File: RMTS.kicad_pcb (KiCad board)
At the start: 2 copper layers, 45 parts, among them J1 USB_B_Mini, J2 Programmer, J3 Screw_Terminal_01x03, J4 Screw_Terminal_01x04, J5 Screw_Terminal_01x02, J6 Screw_Terminal_01x02, J7 MICRO-SD_CARD_SOCKET, J8 CONN_03, Q1 PMV20ENR, U1 ADP2108AUJ-3.3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

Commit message: Finished layout
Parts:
- added C14: 12pF, Capacitor_SMD:C_0805_2012Metric_Pad1.15x1.40mm_HandSolder, F.Cu at (182.9, 102.9)
- added C15: 12pF, Capacitor_SMD:C_0805_2012Metric_Pad1.15x1.40mm_HandSolder, F.Cu at (182.6, 95.2)
- added C16: 0.1uF, Capacitor_SMD:C_0805_2012Metric_Pad1.15x1.40mm_HandSolder, F.Cu at (163.4, 81.9)
- added J10: CONN_02, Connectors:1X02, F.Cu at (141.6, 99.7)
- added J9: CONN_02, Connectors:1X02, F.Cu at (147.3, 99.7)
- added Y2: Crystal_GND24_Small, Crystal:Crystal_SMD_3225-4Pin_3.2x2.5mm, F.Cu at (183.1, 99.1)
- J7: value MICRO-SD_CARD_SOCKET -> Micro_SD_Card_Det_Hirose_DM3AT; footprint Connectors:MICRO-SD-SOCKET -> Connector_Card:microSD_HC_Hirose_DM3AT-SF-PEJM5
- moved C12 14.6 mm to (197.9, 89.5), turned to 180 degrees
- moved C1 11.4 mm to (142.2, 72.0), turned to 90 degrees
- moved R5 10.8 mm to (205.5, 92.1)
- moved TP2 10.0 mm to (151.8, 78.1)
- moved C13 9.17 mm to (201.5, 68.6), turned to 180 degrees
- moved J7 8.60 mm to (167.2, 71.7), turned to 180 degrees
- moved C2 8.26 mm to (153.3, 73.0)
- moved R2 7.92 mm to (146.3, 80.0), turned to 180 degrees
- moved U1 7.15 mm to (146.1, 72.1)
- moved L1 6.96 mm to (146.6, 76.2)
- moved C11 6.47 mm to (202.2, 89.5)
- moved U3 6.37 mm to (199.4, 97.8)
- moved Q1 5.65 mm to (146.4, 95.6)
- moved J1 5.31 mm to (134.6, 73.3)
- moved R8 5.28 mm to (193.7, 97.5)
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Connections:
- net Net-(U2-Pad32) renamed /XTAL1
- net Net-(U2-Pad33) renamed /XTAL2
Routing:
- net +3V3: track 9.50 -> 186.6 mm, vias 0 -> 4
- net GND: track 0.00 -> 124.1 mm, vias 0 -> 17
- net /VBUS: track 0.00 -> 118.0 mm, vias 0 -> 2
- net /DIN: track 0.00 -> 40.0 mm
- net /DOUT: track 0.00 -> 37.9 mm
- net Net-(D2-Pad2): track 0.00 -> 28.3 mm, vias 0 -> 2
- net /USBM: track 0.00 -> 21.7 mm
- net /Fire: track 0.00 -> 20.6 mm, vias 0 -> 2
- net Net-(D1-Pad2): track 0.00 -> 20.0 mm
- net /USBP: track 0.00 -> 16.9 mm
- net Net-(J1-Pad3): track 0.00 -> 15.0 mm
- net Net-(J4-Pad4): track 0.00 -> 14.2 mm
- net Net-(J3-Pad3): track 0.00 -> 14.1 mm
- net Net-(J1-Pad2): track 0.00 -> 12.5 mm
- net /LC0: track 0.00 -> 11.9 mm
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- added copper zone on B.Cu, net GND
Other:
- board outline added: 79.4 x 50.2 mm

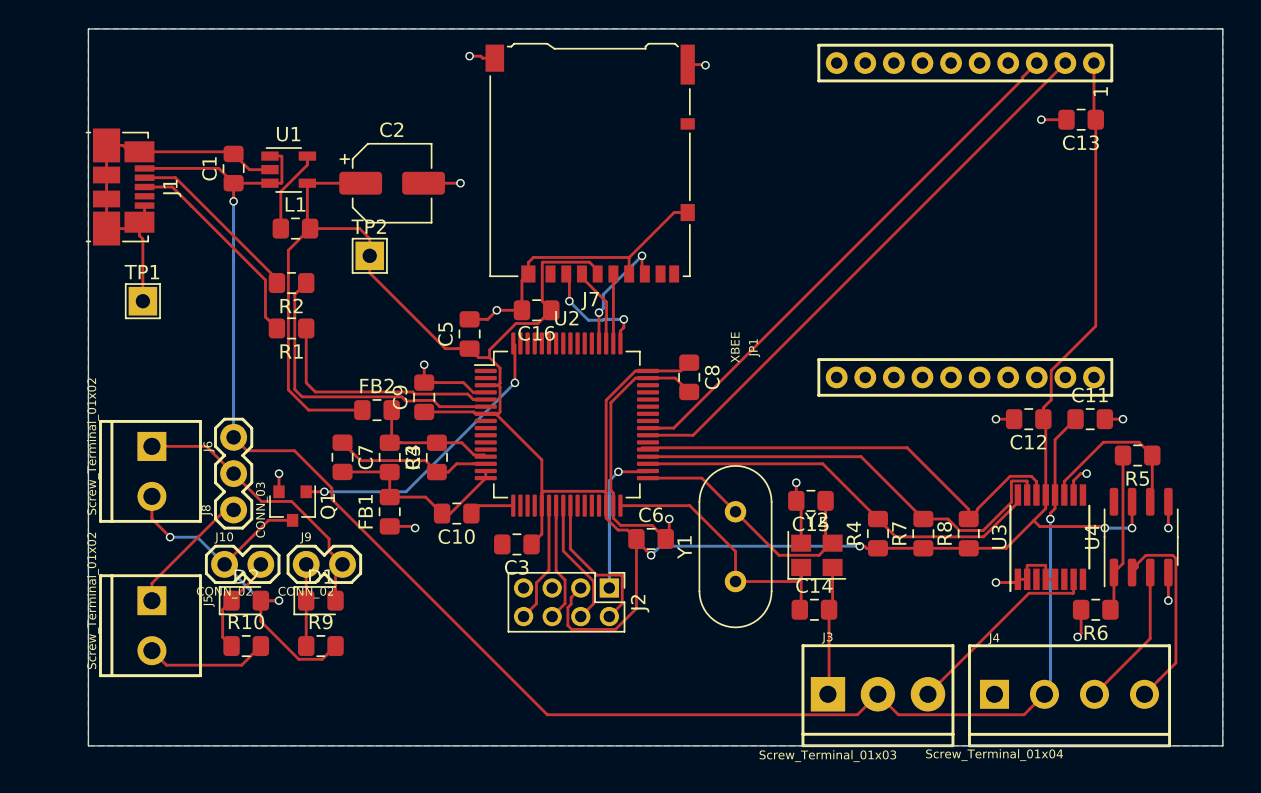
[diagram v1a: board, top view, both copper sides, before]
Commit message: Cleaned up silkscreen
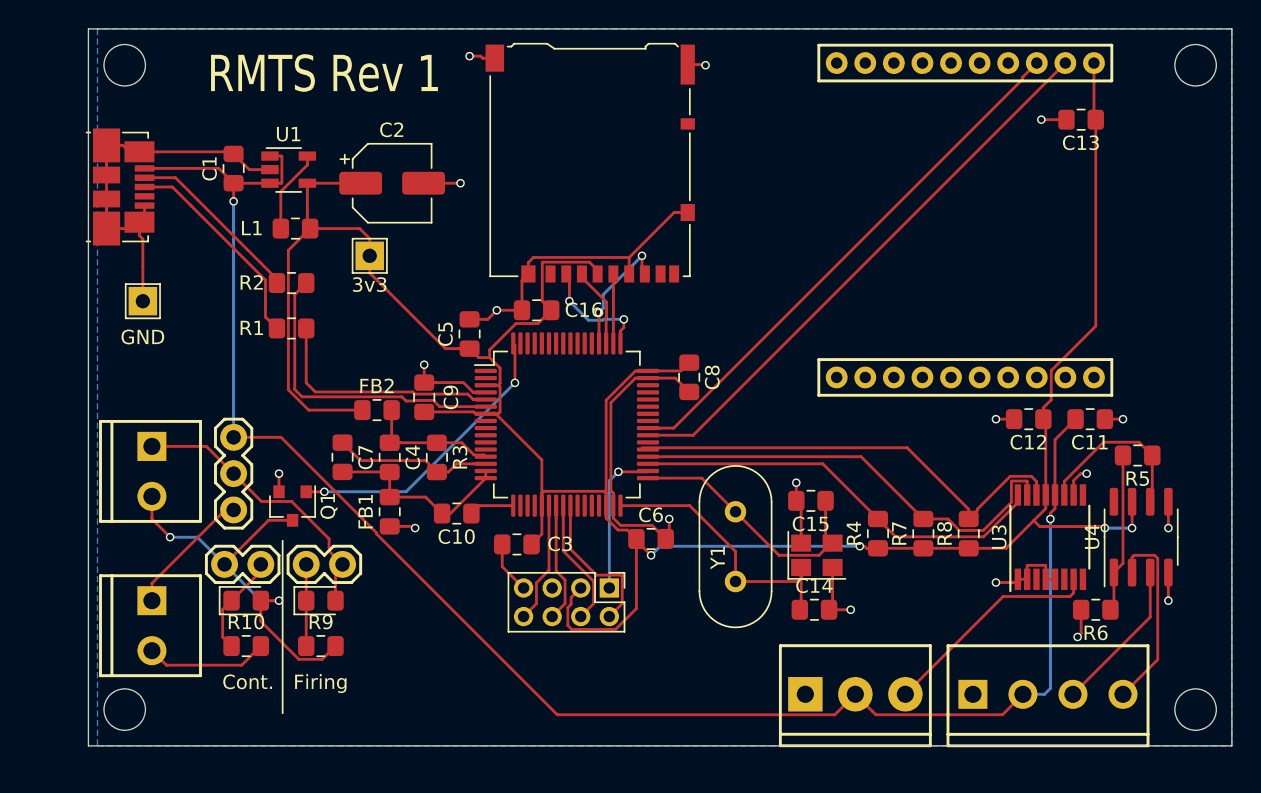
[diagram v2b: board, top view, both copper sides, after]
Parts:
- TP1: value TestPoint -> GND
- TP2: value TestPoint -> 3v3
- moved J3 1.58 mm to (182.2, 108.8)
- moved J4 1.51 mm to (194.0, 108.8)
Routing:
- net Net-(J3-Pad3): track 14.1 -> 15.7 mm
- net GND: track 124.1 -> 123.3 mm, vias 17 -> 18
- net Net-(J4-Pad4): track 14.2 -> 13.5 mm
- net Net-(J4-Pad3): track 10.1 -> 10.8 mm
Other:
- board size 79.4 x 50.2 mm -> 80 x 50.2 mm
- board text added: "Cont."
- board text added: "Firing"
- board text added: "RMTS Rev 1"

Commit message: Added label to screw terminals
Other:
- board text added: "+"
- board text added: "-"
- board text added: "Igniter"
- board text added: "SIG"
- board text added: "SIG+"
- board text added: "SIG-"
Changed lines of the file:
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@@
   (general
     (thickness 1.6)
-    (drawings 12)
+    (drawings 22)
     (tracks 462)
     (zones 0)
@@
     (solder_mask_min_width 0.25)
     (aux_axis_origin 0 0)
-    (visible_elements 7FFFFFFF)
+    (visible_elements 7FFDFFFF)
     (pcbplotparams
       (layerselection 0x010fc_ffffffff)
@@
       (net 10 "Net-(D2-Pad2)") (solder_mask_margin 0.1016))
   )
+  (gr_text Igniter (at 133.858 93.218 -90) (layer B.SilkS)
+    (effects (font (size 1 1) (thickness 0.15)) (justify mirror))
+  )
+  (gr_text + (at 133.985 102.235 90) (layer B.SilkS)
+    (effects (font (size 1 1) (thickness 0.15)) (justify mirror))
+  )
+  (gr_text - (at 133.858 105.791 90) (layer B.SilkS)
+    (effects (font (size 1 1) (thickness 0.15)) (justify mirror))
+  )
+  (gr_text SIG- (at 204.216 110.998) (layer B.SilkS)
+    (effects (font (size 1 1) (thickness 0.15)) (justify mirror))
+  )
+  (gr_text SIG+ (at 200.406 110.998) (layer B.SilkS)
+    (effects (font (size 1 1) (thickness 0.15)) (justify mirror))
+  )
+  (gr_text + (at 197.485 110.998) (layer B.SilkS)
+    (effects (font (size 1 1) (thickness 0.15)) (justify mirror))
+  )
+  (gr_text - (at 193.929 110.998) (layer B.SilkS)
+    (effects (font (size 1 1) (thickness 0.15)) (justify mirror))
+  )
+  (gr_text SIG (at 189.23 111.125) (layer B.SilkS)
+    (effects (font (size 1 1) (thickness 0.15)) (justify mirror))
+  )
+  (gr_text + (at 185.801 111.125) (layer B.SilkS)
+    (effects (font (size 1 1) (thickness 0.15)) (justify mirror))
+  )
+  (gr_text - (at 182.245 111.125) (layer B.SilkS)
+    (effects (font (size 1 1) (thickness 0.15)) (justify mirror))
+  )
   (gr_line (start 145.669 98.044) (end 145.669 110.109) (layer F.SilkS) (width 0.12))

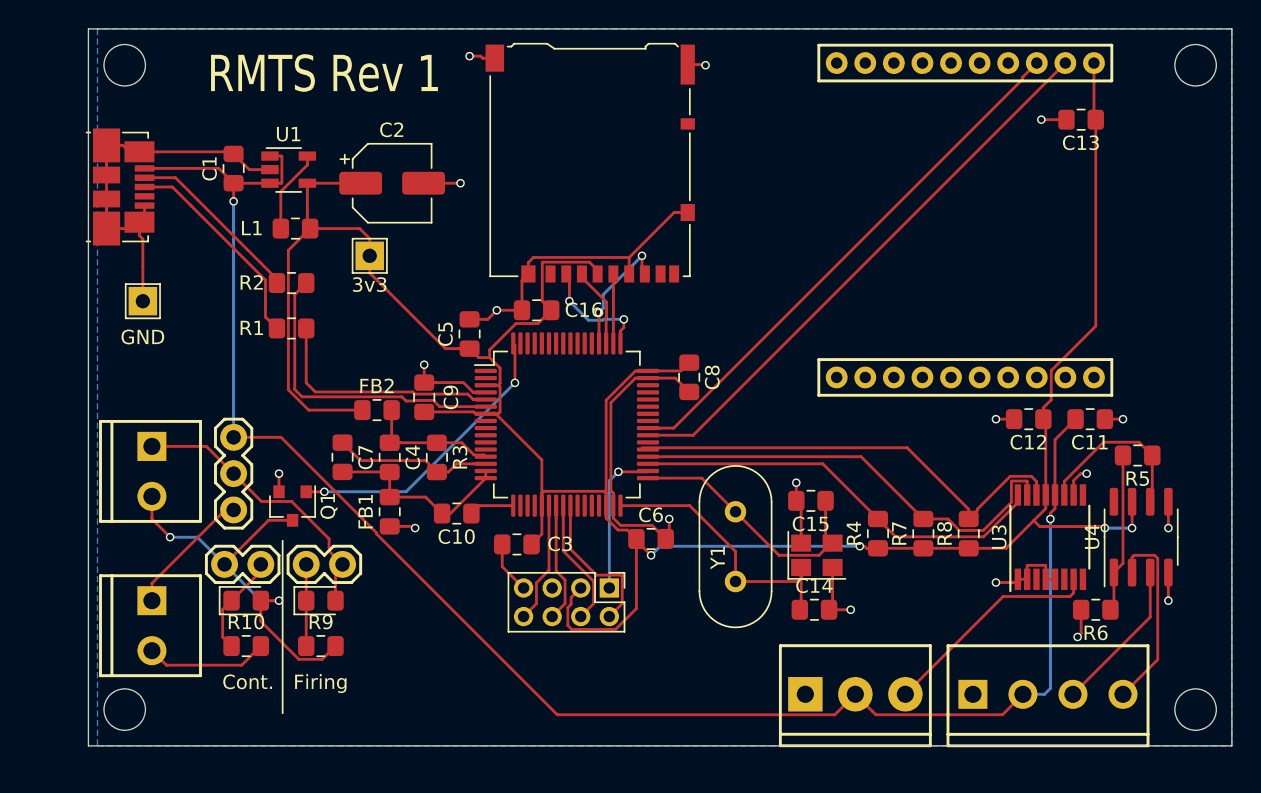
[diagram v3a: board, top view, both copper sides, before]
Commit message: Added 3v3 top plane
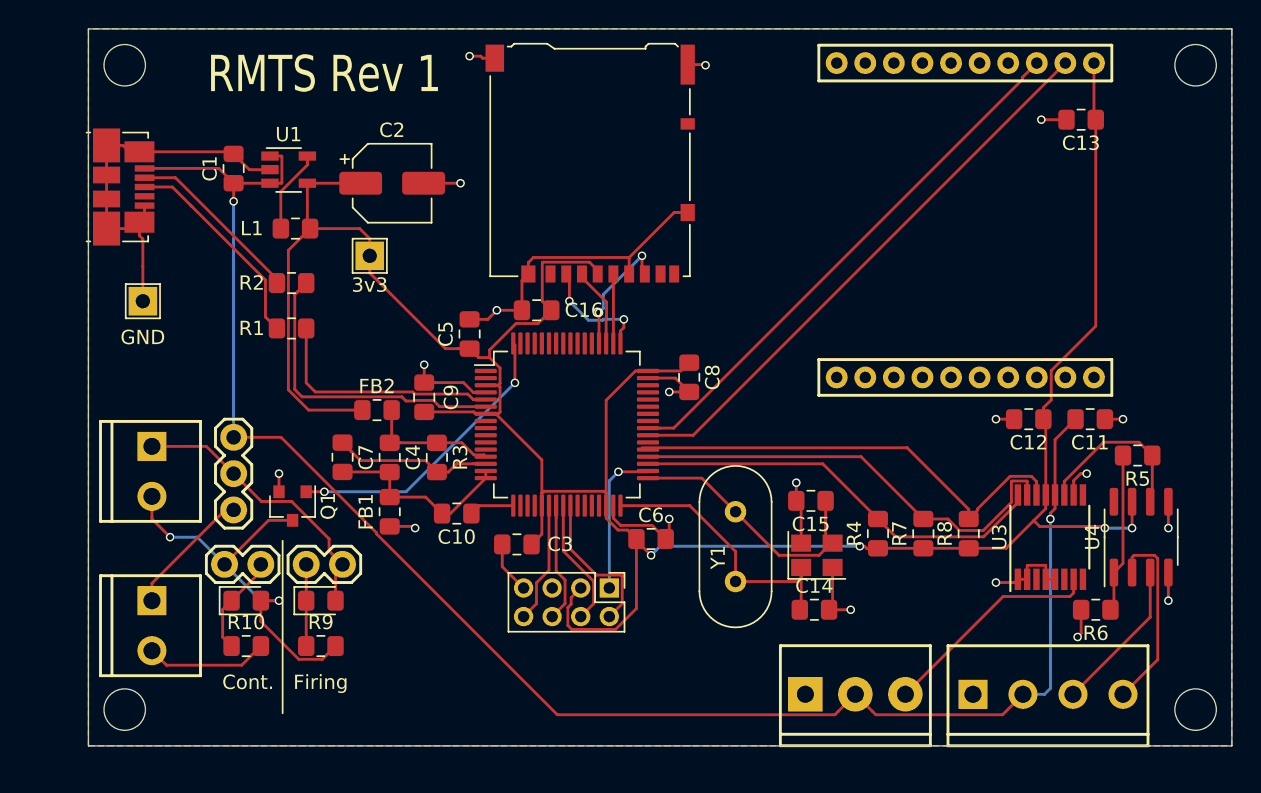
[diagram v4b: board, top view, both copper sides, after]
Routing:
- net GND: track 123.3 -> 114.1 mm, vias 18 -> 19
- added copper zone on F.Cu, net +3V3
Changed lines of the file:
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@@
     (thickness 1.6)
     (drawings 22)
-    (tracks 462)
+    (tracks 459)
     (zones 0)
     (modules 51)
@@
   (segment (start 181.95 95.59) (end 181.61 95.25) (width 0.2) (layer F.Cu) (net 1))
   (segment (start 181.95 98.21) (end 181.95 95.59) (width 0.2) (layer F.Cu) (net 1))
-  (segment (start 170.357001 86.660001) (end 171.232001 86.660001) (width 0.2) (layer F.Cu) (net 1))
-  (segment (start 168.636999 88.380003) (end 170.357001 86.660001) (width 0.2) (layer F.Cu) (net 1))
-  (segment (start 168.636999 94.539999) (end 168.636999 88.380003) (width 0.2) (layer F.Cu) (net 1))
-  (segment (start 168.807001 94.710001) (end 168.636999 94.539999) (width 0.2) (layer F.Cu) (net 1))
-  (segment (start 168.807001 95.585001) (end 168.807001 94.710001) (width 0.2) (layer F.Cu) (net 1))
   (segment (start 173.31348 75.075) (end 174.01348 75.075) (width 0.2) (layer F.Cu) (net 1))
   (segment (start 173.065038 75.075) (end 173.31348 75.075) (width 0.2) (layer F.Cu) (net 1))
@@
   (via (at 185.42 102.87) (size 0.6) (drill 0.4) (layers F.Cu B.Cu) (net 1))
   (segment (start 183.905 102.87) (end 185.42 102.87) (width 0.2) (layer F.Cu) (net 1))
+  (via (at 172.72 87.63) (size 0.6) (drill 0.4) (layers F.Cu B.Cu) (net 1))
+  (segment (start 172.72 87.63) (end 174.117 87.63) (width 0.2) (layer F.Cu) (net 1))
   (segment (start 199.715 90.97) (end 201.15 89.535) (width 0.2) (layer F.Cu) (net 2))
   (segment (start 199.715 94.84) (end 199.715 90.97) (width 0.2) (layer F.Cu) (net 2))
@@
     (polygon
       (pts
-        (xy 132.715 62.23) (xy 132.715 112.395) (xy 212.09 112.395) (xy 212.09 62.23)
+        (xy 132.08 62.23) (xy 132.08 112.395) (xy 212.09 112.395) (xy 212.09 62.23)
       )
     )
+  )
+  (zone (net 3) (net_name +3V3) (layer F.Cu) (hatch edge 0.508)
+    (connect_pads (clearance 0.508))
+    (min_thickness 0.254)
+    (fill yes (arc_segments 32) (thermal_gap 0.508) (thermal_bridge_width 0.508))
+    (polygon
+      (pts
+        (xy 132.08 62.23) (xy 132.08 112.395) (xy 212.09 112.395) (xy 212.09 62.23)
+      )
+    )

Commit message: Changed USB to full size, connected amp enable, cleaned up routing
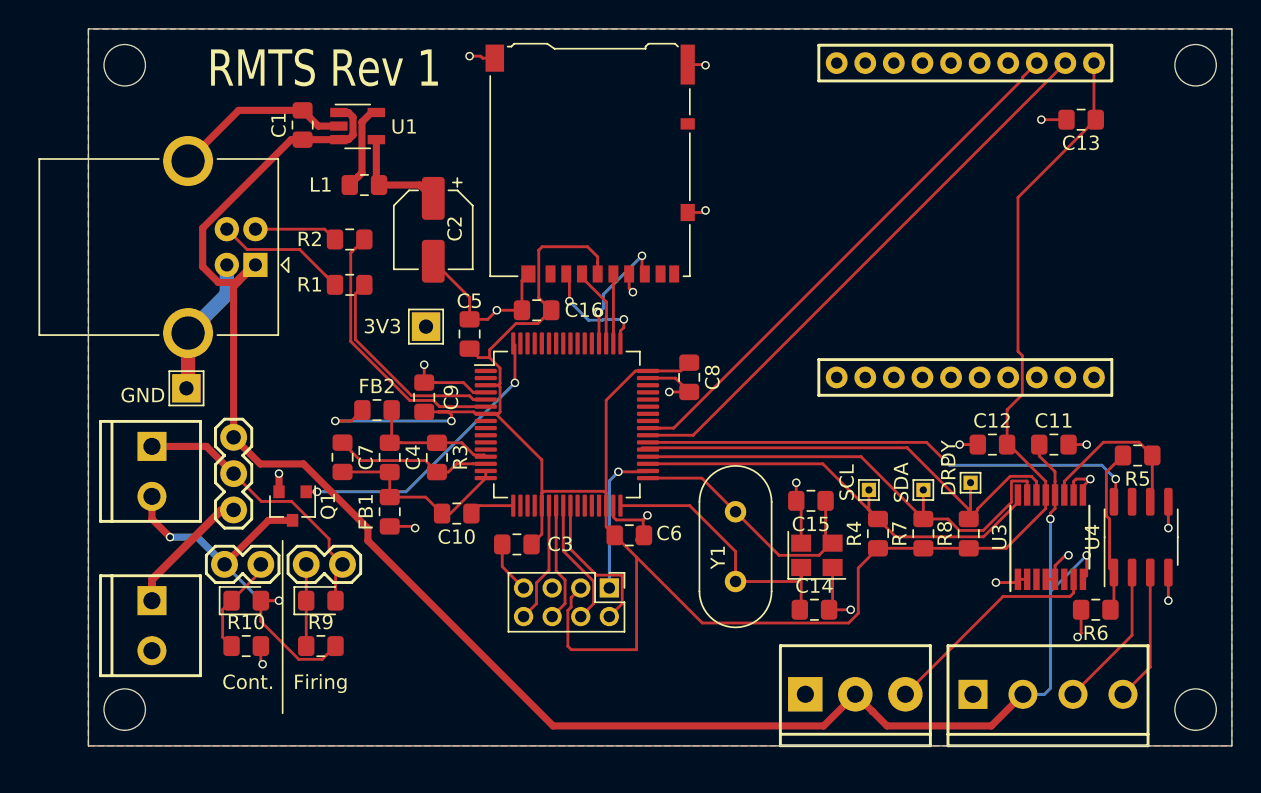
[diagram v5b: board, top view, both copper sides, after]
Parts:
- added DRDY: TestPoint, TestPoint:TestPoint_THTPad_1.0x1.0mm_Drill0.5mm, F.Cu at (193.8, 94.0)
- added SCL: TestPoint, TestPoint:TestPoint_THTPad_1.0x1.0mm_Drill0.5mm, F.Cu at (186.7, 94.5)
- added SDA: TestPoint, TestPoint:TestPoint_THTPad_1.0x1.0mm_Drill0.5mm, F.Cu at (190.5, 94.5)
- J1: value USB_B_Mini -> USB_B; footprint Connector_USB:USB_Micro-B_Molex_47346-0001 -> Connector_USB:USB_B_OST_USB-B1HSxx_Horizontal
- TP2: value 3v3 -> 3V3
- moved J1 10.7 mm to (143.8, 78.7), turned to 180 degrees
- moved TP1 6.82 mm to (138.9, 87.4)
- moved TP2 6.33 mm to (155.7, 83.1)
- moved C1 5.71 mm to (147.1, 69.0)
- moved L1 5.71 mm to (151.4, 73.2)
- moved U1 5.71 mm to (150.9, 69.0)
- moved R1 5.08 mm to (150.4, 80.1)
- moved R2 5.08 mm to (150.4, 77.0)
- moved C2 4.35 mm to (156.2, 76.3), turned to 270 degrees
- moved C11 3.10 mm to (199.6, 91.3)
- moved C12 3.10 mm to (195.3, 91.3)
- moved C6 1.55 mm to (169.9, 97.7)
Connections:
- J1 pad 4: Net-(J1-Pad4) -> GND
- U2 pad 38: Net-(U2-Pad38) -> /AMP_EN
- U3 pad 8: Net-(U3-Pad8) -> /VBUS
- U3 pad 9: Net-(U3-Pad9) -> GND
- U4 pad 2: Net-(J4-Pad4) -> Net-(J4-Pad3)
- U4 pad 3: Net-(J4-Pad3) -> Net-(J4-Pad4)
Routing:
- net /AMP_EN: track 0.00 -> 35.4 mm, vias 0 -> 2
- net GND: track 114.1 -> 91.0 mm, vias 19 -> 22
- net +3V3: track 186.6 -> 169.5 mm, vias 4 -> 2
- net /VBUS: track 117.6 -> 128.1 mm
- net Net-(J5-Pad1): track 9.06 -> 18.3 mm
- net Net-(J1-Pad2): track 12.5 -> 5.87 mm
- net Net-(J1-Pad3): track 15.0 -> 9.18 mm
- net Net-(J4-Pad4): track 13.5 -> 9.31 mm
- net /ASCL: track 29.5 -> 32.4 mm
- net /USBM: track 21.7 -> 18.9 mm
- net /ADRDY: track 32.4 -> 35.0 mm
- net /ASDA: track 31.9 -> 33.9 mm
- net /USBP: track 16.9 -> 14.9 mm
- net Net-(J4-Pad3): track 10.8 -> 10.2 mm
